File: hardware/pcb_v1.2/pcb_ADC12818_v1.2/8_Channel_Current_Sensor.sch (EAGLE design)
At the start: 46 parts, among them Q1 BSS138, Q2 BSS138, SW1 DIP-SLIDE-SWITCH-EG1218

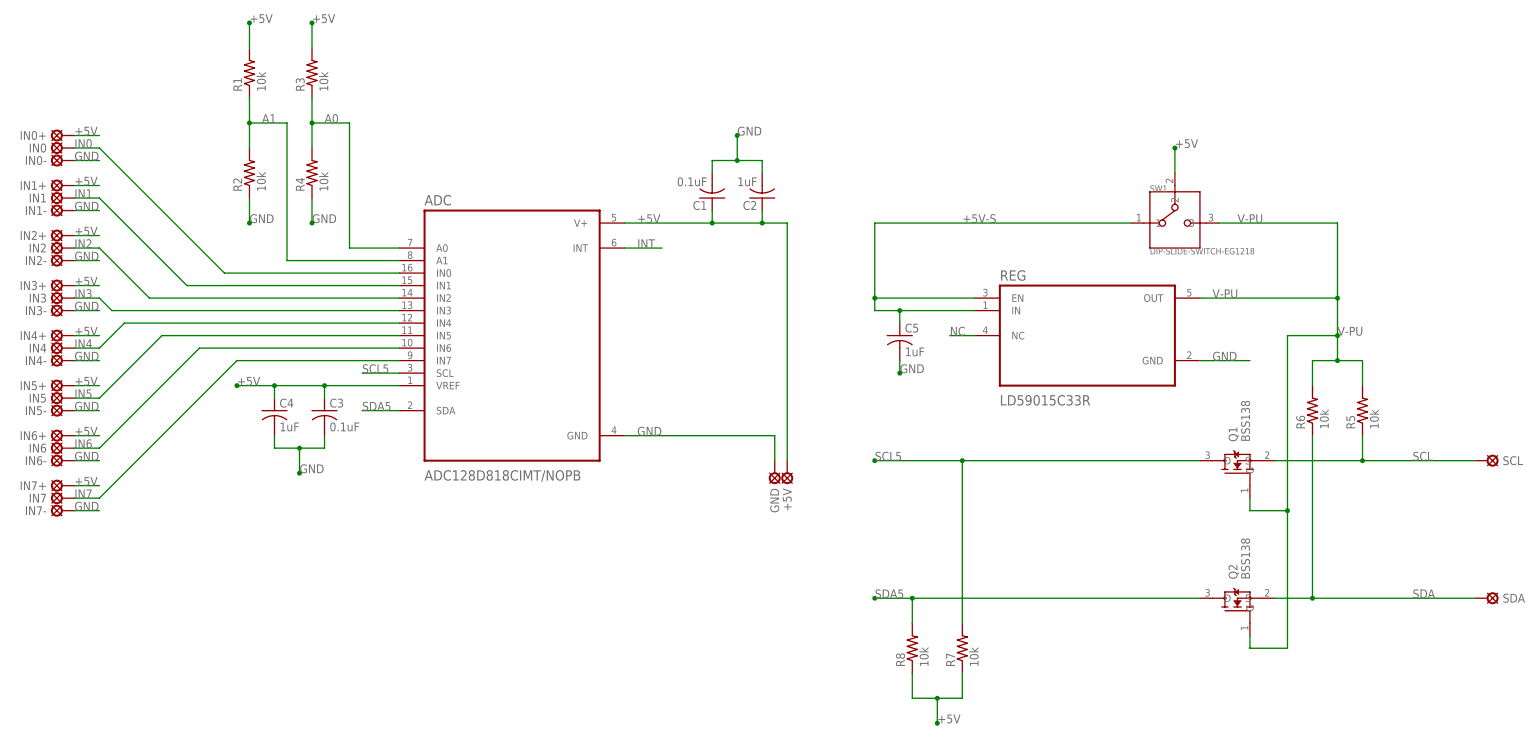
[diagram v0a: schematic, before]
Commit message: New PCB designs, reorganized files, removed clutter
Added pcb v1.2 the final draft of the ADC12818 board.
Added pcb v2.0 the new board boased on the MAX1614EE+ ADC
Added datasheet for MAX ADC
Renamed folders to have consistent naming scheme
Removed unncessary tempoary files
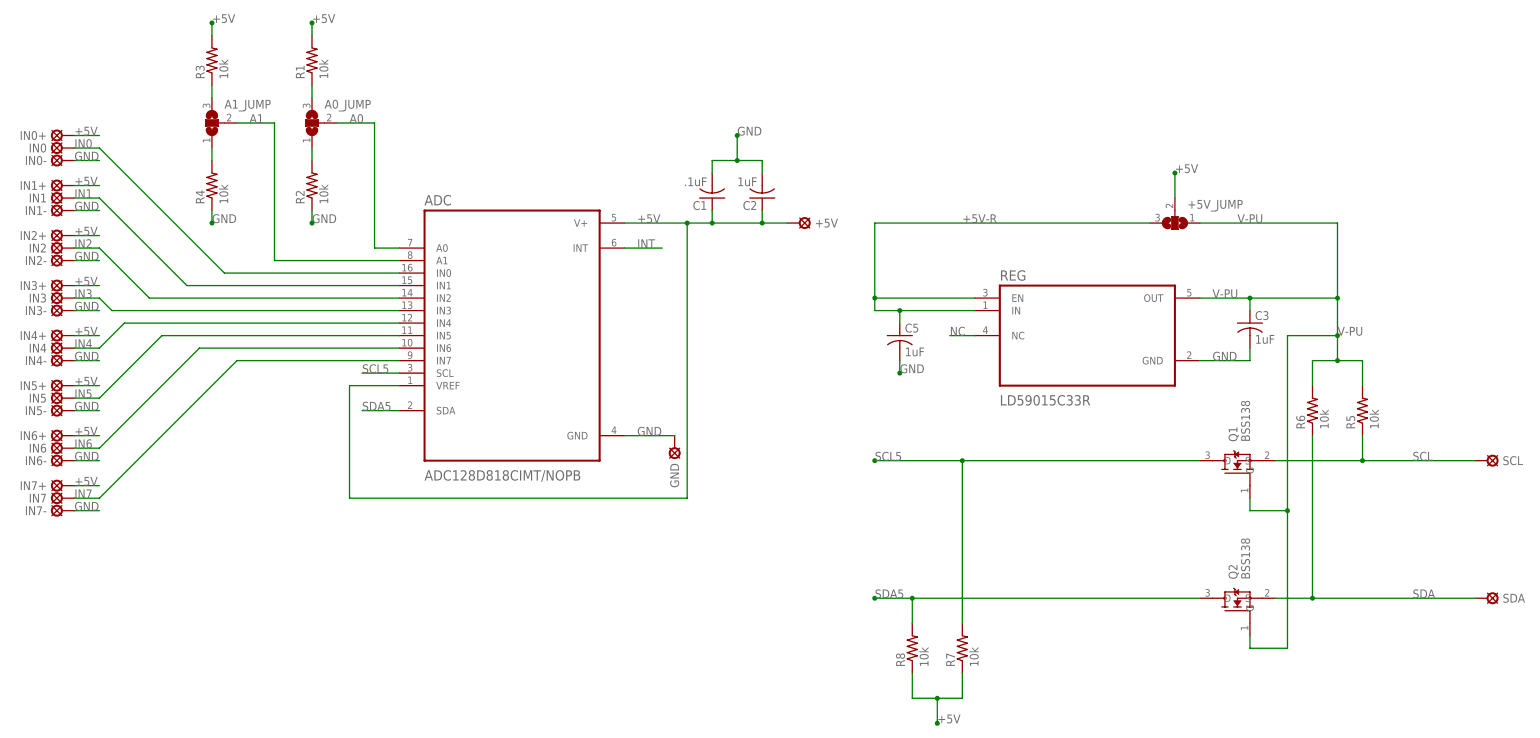
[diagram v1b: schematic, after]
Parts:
- removed C4: 1uF, resistor:C-USC0603
- removed SW1: DIP-SLIDE-SWITCH-EG1218, EG1218-DIP-SLIDE-SWITCH:DIP-SLIDE-SWITCH-EG1218
- added +5V_JUMP, A0_JUMP, A1_JUMP: (no value), jumper:SJ2W
- C1: value 0.1uF -> .1uF
- C3: value 0.1uF -> 1uF
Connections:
- removed net +5V-S: C5.1, REG.EN, REG.IN, SW1.1
- new net +5V-R: +5V_JUMP.3, C5.1, REG.EN, REG.IN
- new net N$1: A1_JUMP.3, R3.1
- new net N$2: A1_JUMP.1, R4.2
- new net N$3: A0_JUMP.1, R2.2
- new net N$4: A0_JUMP.3, R1.1
- net +5V: now also +5V_JUMP.2; no longer C3.1, C4.1, SW1.2
- net A0: now also A0_JUMP.2; no longer R3.1, R4.2
- net A1: now also A1_JUMP.2; no longer R1.1, R2.2
- net GND: no longer C4.2
- net V-PU: now also +5V_JUMP.1, C3.1; no longer SW1.3
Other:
- moved on the sheet: +5V, C3, GND, R1, R2, R3, R4
